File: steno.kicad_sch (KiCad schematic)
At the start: 16 parts, among them J1 USB_C_Receptacle_USB2.0_14P, U2 AP2127N-3.3, U3 W25Q16JVSS

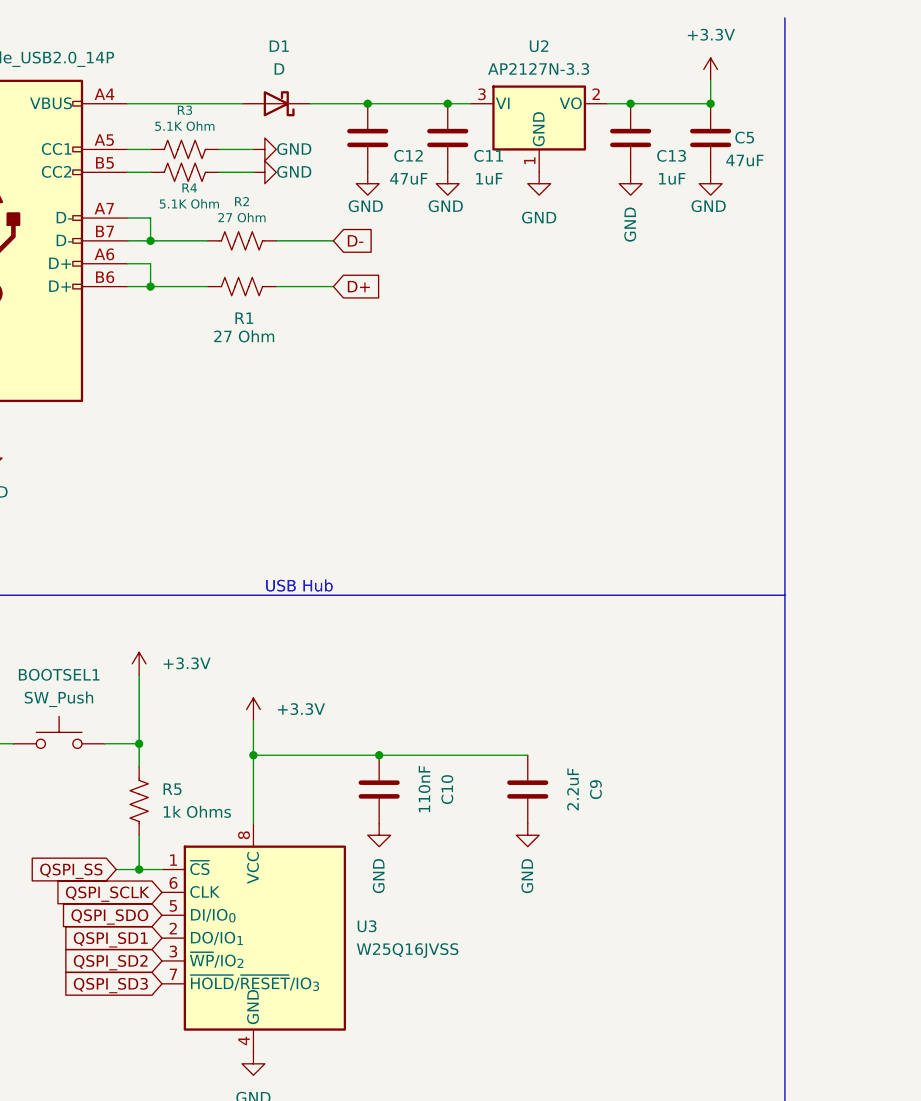
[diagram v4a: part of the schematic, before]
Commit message: Fixing buttons / Transitioning to new computer.
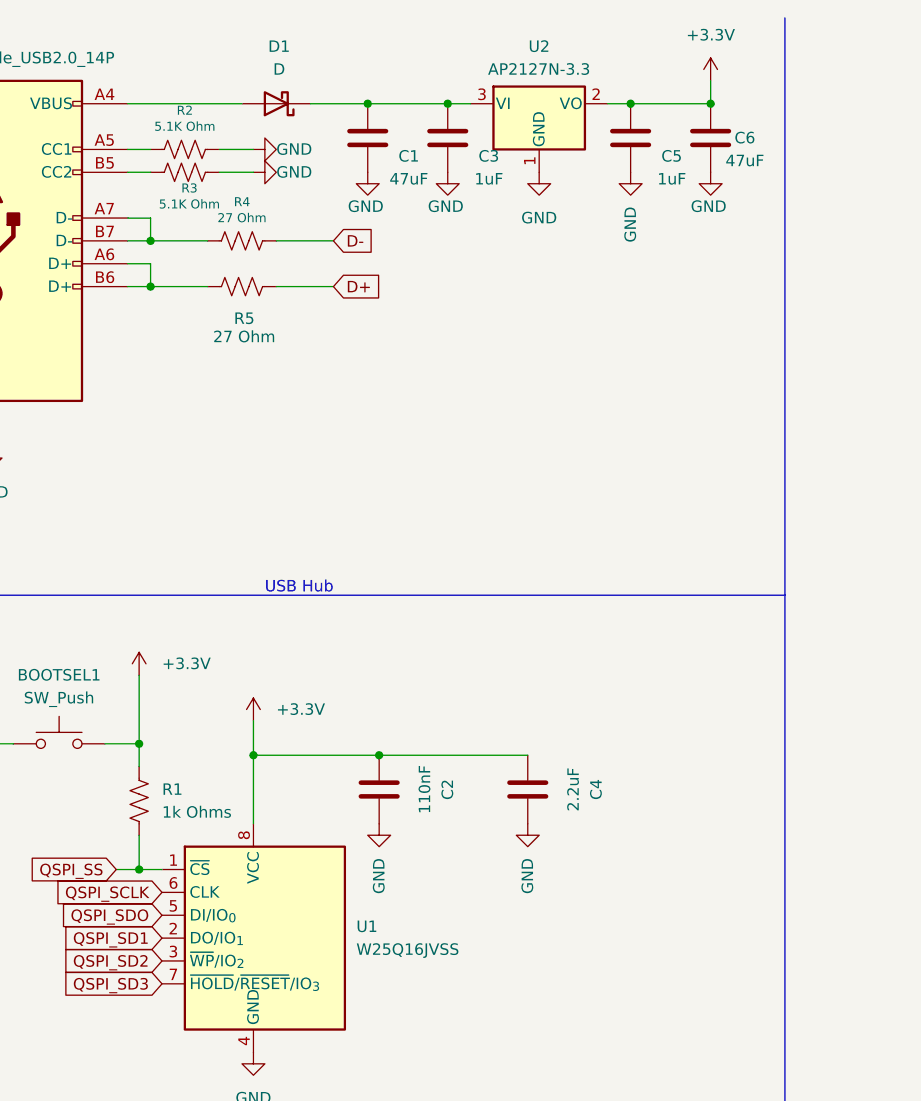
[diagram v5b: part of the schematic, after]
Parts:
- BOOTSEL1: footprint ScottoKeebs_Components:Button_MJTP1243 -> 3rd_party_footprints:SW4_PTS815 SJM 250 SMTR LFS_CNK
- renumbered C12 to C1, C10 to C2, C11 to C3, C9 to C4, C13 to C5, C5 to C6, R5 to R1, R3 to R2, R4 to R3, R2 to R4, R1 to R5, U3 to U1
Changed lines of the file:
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@@
 		(in_pos_files yes)
 		(dnp no)
-		(property "Reference" "C5"
+		(property "Reference" "C6"
 			(at 113.03 25.4 0)
 			(show_name no)
@@
 			(project "steno"
 				(path "/238e1d3b-9ec5-448b-85c7-386a29cd2631"
-					(reference "C5")
+					(reference "C6")
 					(unit 1)
 				)
@@
 		(in_pos_files yes)
 		(dnp no)
-		(property "Reference" "R3"
+		(property "Reference" "R2"
 			(at 50.8 22.352 90)
 			(show_name no)
@@
 			(project "steno"
 				(path "/238e1d3b-9ec5-448b-85c7-386a29cd2631"
-					(reference "R3")
+					(reference "R2")
 					(unit 1)
 				)
@@
 		(in_pos_files yes)
 		(dnp no)
-		(property "Reference" "C12"
+		(property "Reference" "C1"
 			(at 75.692 27.432 0)
 			(show_name no)
@@
 			(project "steno"
 				(path "/238e1d3b-9ec5-448b-85c7-386a29cd2631"
-					(reference "C12")
+					(reference "C1")
 					(unit 1)
 				)
@@
 		(in_pos_files yes)
 		(dnp no)
-		(property "Reference" "C13"
+		(property "Reference" "C5"
 			(at 104.902 27.432 0)
 			(show_name no)
@@
 			(project "steno"
 				(path "/238e1d3b-9ec5-448b-85c7-386a29cd2631"
-					(reference "C13")
+					(reference "C5")
 					(unit 1)
 				)
@@
 		(in_pos_files yes)
 		(dnp no)
-		(property "Reference" "C11"
+		(property "Reference" "C3"
 			(at 84.582 27.432 0)
 			(show_name no)
@@
 			(project "steno"
 				(path "/238e1d3b-9ec5-448b-85c7-386a29cd2631"
-					(reference "C11")
+					(reference "C3")
 					(unit 1)
 				)
@@
 		(in_pos_files yes)
 		(dnp no)
-		(property "Reference" "#PWR023"
+		(property "Reference" "#PWR02"
 			(at 26.67 102.87 0)
 			(hide yes)
@@
 			(project "steno"
 				(path "/238e1d3b-9ec5-448b-85c7-386a29cd2631"
-					(reference "#PWR023")
+					(reference "#PWR02")
 					(unit 1)
 				)
@@
 		(in_pos_files yes)
 		(dnp no)
-		(property "Reference" "R1"
+		(property "Reference" "R5"
 			(at 57.404 45.466 90)
 			(show_name no)
@@
 			(project "steno"
 				(path "/238e1d3b-9ec5-448b-85c7-386a29cd2631"
-					(reference "R1")
+					(reference "R5")
 					(unit 1)
 				)
@@
 		(in_pos_files yes)
 		(dnp no)
-		(property "Reference" "R4"
+		(property "Reference" "R3"
 			(at 51.308 30.988 90)
 			(show_name no)
@@
 			(project "steno"
 				(path "/238e1d3b-9ec5-448b-85c7-386a29cd2631"
-					(reference "R4")
+					(reference "R3")
 					(unit 1)
 				)
@@
 		(dnp no)
 		(fields_autoplaced yes)
-		(property "Reference" "#PWR027"
+		(property "Reference" "#PWR014"
 			(at 100.33 35.56 0)
 			(hide yes)
@@
 			(project "steno"
 				(path "/238e1d3b-9ec5-448b-85c7-386a29cd2631"
-					(reference "#PWR027")
+					(reference "#PWR014")
 					(unit 1)
 				)
@@
 		(in_pos_files yes)
 		(dnp no)
-		(property "Reference" "#PWR015"
+		(property "Reference" "#PWR06"
 			(at 64.77 29.21 0)
 			(hide yes)
@@
 			(project "steno"
 				(path "/238e1d3b-9ec5-448b-85c7-386a29cd2631"
-					(reference "#PWR015")
+					(reference "#PWR06")
 					(unit 1)
 				)
@@
 		(dnp no)
 		(fields_autoplaced yes)
-		(property "Reference" "#PWR024"
+		(property "Reference" "#PWR04"
 			(at 45.72 88.9 0)
 			(hide yes)
@@
 			(project "steno"
 				(path "/238e1d3b-9ec5-448b-85c7-386a29cd2631"
-					(reference "#PWR024")
+					(reference "#PWR04")
 					(unit 1)
 				)
@@
 		(dnp no)
 		(fields_autoplaced yes)
-		(property "Reference" "#PWR022"
+		(property "Reference" "#PWR010"
 			(at 72.39 107.95 0)
 			(hide yes)
@@
 			(project "steno"
 				(path "/238e1d3b-9ec5-448b-85c7-386a29cd2631"
-					(reference "#PWR022")
+					(reference "#PWR010")
 					(unit 1)
 				)
@@
 		(dnp no)
 		(fields_autoplaced yes)
-		(property "Reference" "#PWR011"
+		(property "Reference" "#PWR01"
 			(at 21.59 66.04 0)
 			(hide yes)
@@
 			(project "steno"
 				(path "/238e1d3b-9ec5-448b-85c7-386a29cd2631"
-					(reference "#PWR011")
+					(reference "#PWR01")
 					(unit 1)
 				)
@@
 		(dnp no)
 		(fields_autoplaced yes)
-		(property "Reference" "R5"
+		(property "Reference" "R1"
 			(at 48.26 97.7899 0)
 			(show_name no)
@@
 			(project "steno"
 				(path "/238e1d3b-9ec5-448b-85c7-386a29cd2631"
-					(reference "R5")
+					(reference "R1")
 					(unit 1)
 				)
@@
 		(in_pos_files yes)
 		(dnp no)
-		(property "Reference" "R2"
+		(property "Reference" "R4"
 			(at 57.15 32.512 90)
 			(show_name no)
@@
 			(project "steno"
 				(path "/238e1d3b-9ec5-448b-85c7-386a29cd2631"
-					(reference "R2")
+					(reference "R4")
 					(unit 1)
 				)
@@
 		(dnp no)
 		(fields_autoplaced yes)
-		(property "Reference" "#PWR010"
+		(property "Reference" "#PWR013"
 			(at 90.17 35.56 0)
 			(hide yes)
@@
 			(project "steno"
 				(path "/238e1d3b-9ec5-448b-85c7-386a29cd2631"
-					(reference "#PWR010")
+					(reference "#PWR013")
 					(unit 1)
 				)
@@
 		(dnp no)
 		(fields_autoplaced yes)
-		(property "Reference" "C10"
+		(property "Reference" "C2"
 			(at 80.01 97.79 90)
 			(show_name no)
@@
 			(project "steno"
 				(path "/238e1d3b-9ec5-448b-85c7-386a29cd2631"
-					(reference "C10")
+					(reference "C2")
 					(unit 1)
 				)
@@
 			)
 		)
-		(property "Footprint" "ScottoKeebs_Components:Button_MJTP1243"
+		(property "Footprint" "3rd_party_footprints:SW4_PTS815 SJM 250 SMTR LFS_CNK"
 			(at 36.83 87.63 0)
 			(hide yes)
@@
 		(dnp no)
 		(fields_autoplaced yes)
-		(property "Reference" "#PWR019"
+		(property "Reference" "#PWR07"
 			(at 58.42 93.98 0)
 			(hide yes)
@@
 			(project "steno"
 				(path "/238e1d3b-9ec5-448b-85c7-386a29cd2631"
-					(reference "#PWR019")
+					(reference "#PWR07")
 					(unit 1)
 				)
@@
 		(in_pos_files yes)
 		(dnp no)
-		(property "Reference" "#PWR014"
+		(property "Reference" "#PWR05"
 			(at 64.77 26.67 0)
 			(hide yes)
@@
 			(project "steno"
 				(path "/238e1d3b-9ec5-448b-85c7-386a29cd2631"
-					(reference "#PWR014")
+					(reference "#PWR05")
 					(unit 1)
 				)
@@
 		(in_pos_files yes)
 		(dnp no)
-		(property "Reference" "#PWR025"
+		(property "Reference" "#PWR011"
 			(at 80.01 35.56 0)
 			(hide yes)
@@
 			(project "steno"
 				(path "/238e1d3b-9ec5-448b-85c7-386a29cd2631"
-					(reference "#PWR025")
+					(reference "#PWR011")
 					(unit 1)
 				)
@@
 		(dnp no)
 		(fields_autoplaced yes)
-		(property "Reference" "C9"
+		(property "Reference" "C4"
 			(at 96.52 97.79 90)
 			(show_name no)
@@
 			(project "steno"
 				(path "/238e1d3b-9ec5-448b-85c7-386a29cd2631"
-					(reference "C9")
+					(reference "C4")
 					(unit 1)
 				)
@@
 		(dnp no)
 		(fields_autoplaced yes)
-		(property "Reference" "#PWR021"
+		(property "Reference" "#PWR012"
 			(at 88.9 107.95 0)
 			(hide yes)
@@
 			(project "steno"
 				(path "/238e1d3b-9ec5-448b-85c7-386a29cd2631"
-					(reference "#PWR021")
+					(reference "#PWR012")
 					(unit 1)
 				)
@@
 		(in_pos_files yes)
 		(dnp no)
-		(property "Reference" "#PWR026"
+		(property "Reference" "#PWR09"
 			(at 71.12 35.56 0)
 			(hide yes)
@@
 			(project "steno"
 				(path "/238e1d3b-9ec5-448b-85c7-386a29cd2631"
-					(reference "#PWR026")
+					(reference "#PWR09")
 					(unit 1)
 				)
@@
 		(in_pos_files yes)
 		(dnp no)
-		(property "Reference" "#PWR013"
+		(property "Reference" "#PWR016"
 			(at 109.22 35.56 0)
 			(hide yes)
@@
 			(project "steno"
 				(path "/238e1d3b-9ec5-448b-85c7-386a29cd2631"
-					(reference "#PWR013")
+					(reference "#PWR016")
 					(unit 1)
 				)
@@
 		(dnp no)
 		(fields_autoplaced yes)
-		(property "Reference" "U3"
+		(property "Reference" "U1"
 			(at 69.85 113.0299 0)
 			(show_name no)
@@
 			(project "steno"
 				(path "/238e1d3b-9ec5-448b-85c7-386a29cd2631"
-					(reference "U3")
+					(reference "U1")
 					(unit 1)
 				)
@@
 		(dnp no)
 		(fields_autoplaced yes)
-		(property "Reference" "#PWR020"
+		(property "Reference" "#PWR08"
 			(at 58.42 133.35 0)
 			(hide yes)
@@
 			(project "steno"
 				(path "/238e1d3b-9ec5-448b-85c7-386a29cd2631"
-					(reference "#PWR020")
+					(reference "#PWR08")
 					(unit 1)
 				)
@@
 		(dnp no)
 		(fields_autoplaced yes)
-		(property "Reference" "#PWR012"
+		(property "Reference" "#PWR015"
 			(at 109.22 22.86 0)
 			(hide yes)
@@
 			(project "steno"
 				(path "/238e1d3b-9ec5-448b-85c7-386a29cd2631"
-					(reference "#PWR012")
-					(unit 1)
-				)
+					(reference "#PWR015")
+					(unit 1)
+				)

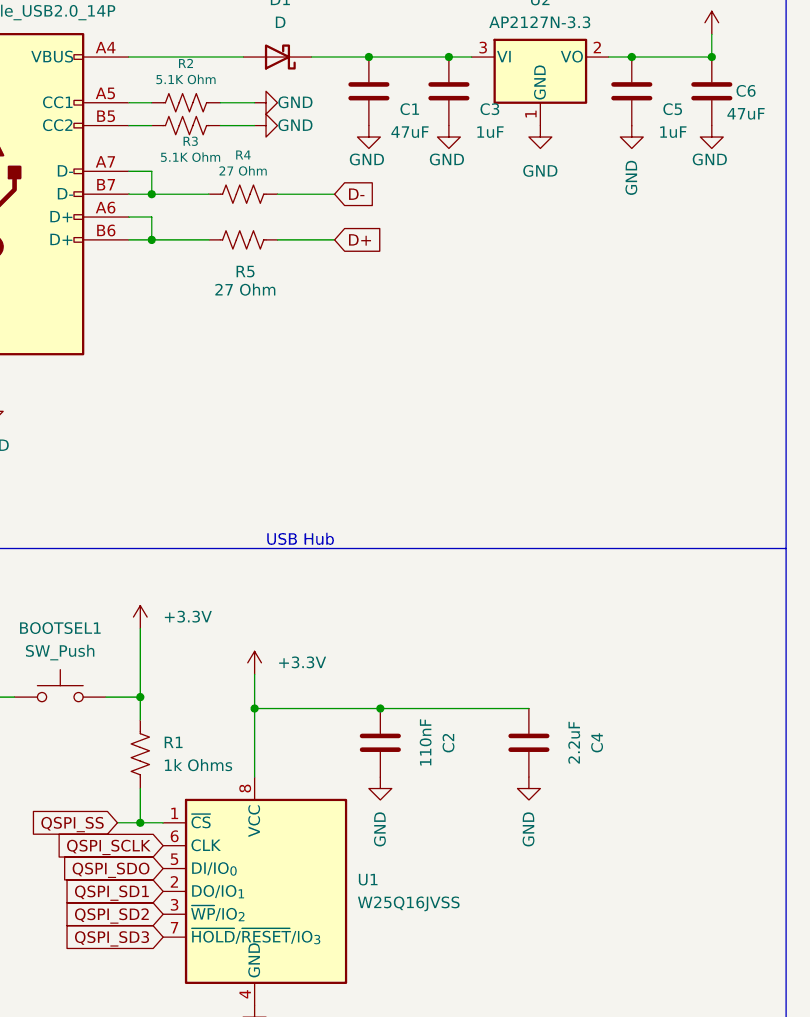
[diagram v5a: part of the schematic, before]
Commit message: added status LED / Potential final changes
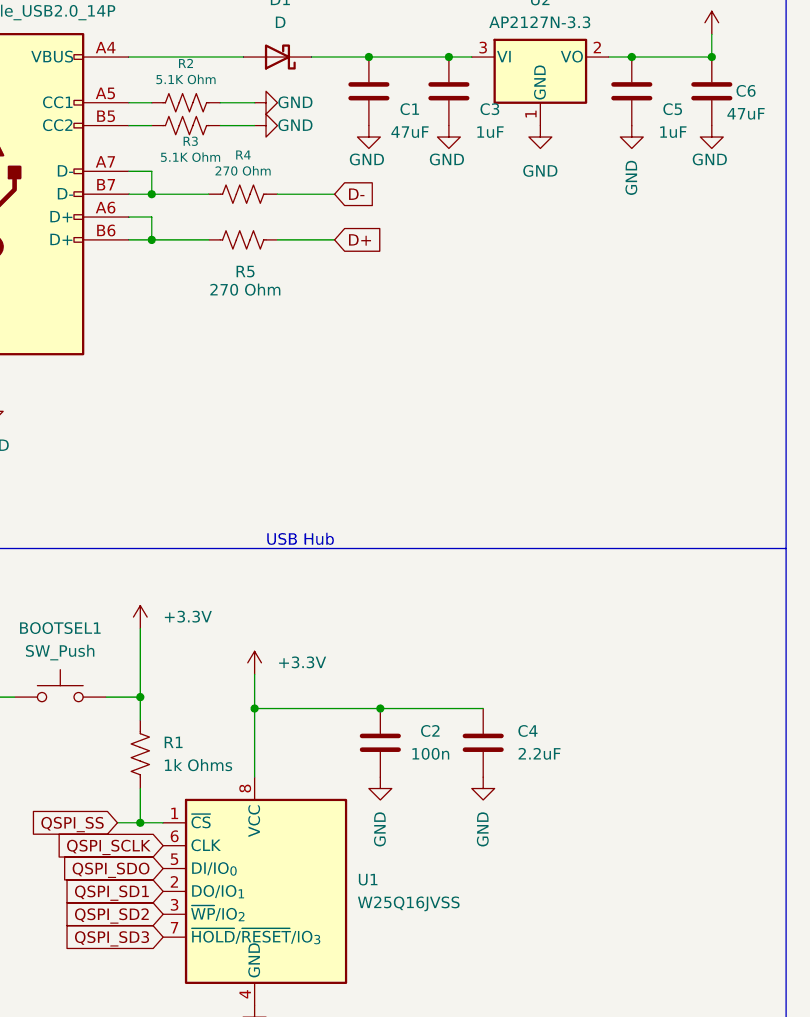
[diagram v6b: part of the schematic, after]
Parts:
- C2: value 110nF -> 100n
- R4, R5: value 27 Ohm -> 270 Ohm
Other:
- moved on the sheet: C4
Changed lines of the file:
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@@
+	)
+	(junction
+		(at 80.01 21.59)
+		(diameter 0)
+		(color 0 0 0 0)
+	)
+	(junction
+		(at 71.12 21.59)
+		(diameter 0)
+		(color 0 0 0 0)
+	)
+	(junction
+		(at 58.42 93.98)
+		(diameter 0)
+		(color 0 0 0 0)
+	)
+	(junction
+		(at 46.99 36.83)
+		(diameter 0)
+		(color 0 0 0 0)
+	)
+	(junction
+		(at 45.72 106.68)
+		(diameter 0)
+		(color 0 0 0 0)
 	)
 	(junction
@@
 	)
 	(junction
-		(at 80.01 21.59)
-		(diameter 0)
-		(color 0 0 0 0)
-	)
-	(junction
-		(at 71.12 21.59)
-		(diameter 0)
-		(color 0 0 0 0)
-	)
-	(junction
-		(at 58.42 93.98)
-		(diameter 0)
-		(color 0 0 0 0)
-	)
-	(junction
-		(at 46.99 36.83)
-		(diameter 0)
-		(color 0 0 0 0)
-	)
-	(junction
-		(at 45.72 106.68)
-		(diameter 0)
-		(color 0 0 0 0)
-	)
-	(junction
 		(at 45.72 92.71)
 		(diameter 0)
@@
 	(wire
 		(pts
-			(xy 72.39 93.98) (xy 88.9 93.98)
+			(xy 72.39 93.98) (xy 83.82 93.98)
 		)
 		(stroke
@@
 			)
 		)
-		(property "Value" "27 Ohm"
+		(property "Value" "270 Ohm"
 			(at 57.404 47.498 90)
 			(show_name no)
@@
 			)
 		)
-		(property "Value" "27 Ohm"
+		(property "Value" "270 Ohm"
 			(at 57.15 34.29 90)
 			(show_name no)
@@
 		(in_pos_files yes)
 		(dnp no)
-		(fields_autoplaced yes)
 		(property "Reference" "C2"
-			(at 80.01 97.79 90)
-			(show_name no)
-			(do_not_autoplace no)
-			(effects
-				(font
-					(size 1.27 1.27)
-				)
-			)
-		)
-		(property "Value" "110nF"
-			(at 77.47 97.79 90)
+			(at 77.978 96.52 0)
+			(show_name no)
+			(do_not_autoplace no)
+			(effects
+				(font
+					(size 1.27 1.27)
+				)
+			)
+		)
+		(property "Value" "100n"
+			(at 77.978 99.06 0)
 			(show_name no)
 			(do_not_autoplace no)
@@
 	(symbol
 		(lib_id "Device:C")
-		(at 88.9 97.79 0)
+		(at 83.82 97.79 0)
 		(unit 1)
 		(body_style 1)
@@
 		(fields_autoplaced yes)
 		(property "Reference" "C4"
-			(at 96.52 97.79 90)
-			(show_name no)
-			(do_not_autoplace no)
-			(effects
-				(font
-					(size 1.27 1.27)
-				)
+			(at 87.63 96.5199 0)
+			(show_name no)
+			(do_not_autoplace no)
+			(effects
+				(font
+					(size 1.27 1.27)
+				)
+				(justify left)
 			)
 		)
 		(property "Value" "2.2uF"
-			(at 93.98 97.79 90)
-			(show_name no)
-			(do_not_autoplace no)
-			(effects
-				(font
-					(size 1.27 1.27)
-				)
+			(at 87.63 99.0599 0)
+			(show_name no)
+			(do_not_autoplace no)
+			(effects
+				(font
+					(size 1.27 1.27)
+				)
+				(justify left)
 			)
 		)
 		(property "Footprint" "Capacitor_SMD:C_0402_1005Metric_Pad0.74x0.62mm_HandSolder"
-			(at 89.8652 101.6 0)
+			(at 84.7852 101.6 0)
 			(hide yes)
 			(show_name no)
@@
 		)
 		(property "Datasheet" ""
-			(at 88.9 97.79 0)
+			(at 83.82 97.79 0)
 			(hide yes)
 			(show_name no)
@@
 		)
 		(property "Description" "Unpolarized capacitor"
-			(at 88.9 97.79 0)
+			(at 83.82 97.79 0)
 			(hide yes)
 			(show_name no)
@@
 	(symbol
 		(lib_id "power:GND")
-		(at 88.9 101.6 0)
+		(at 83.82 101.6 0)
 		(unit 1)
 		(body_style 1)
@@
 		(fields_autoplaced yes)
 		(property "Reference" "#PWR012"
-			(at 88.9 107.95 0)
+			(at 83.82 107.95 0)
 			(hide yes)
 			(show_name no)
@@
 		)
 		(property "Value" "GND"
-			(at 88.9001 105.41 90)
+			(at 83.8201 105.41 90)
 			(show_name no)
 			(do_not_autoplace no)
@@
 		)
 		(property "Footprint" ""
-			(at 88.9 101.6 0)
+			(at 83.82 101.6 0)
 			(hide yes)
 			(show_name no)
@@
 		)
 		(property "Datasheet" ""
-			(at 88.9 101.6 0)
+			(at 83.82 101.6 0)
 			(hide yes)
 			(show_name no)
@@
 		)
 		(property "Description" "Power symbol creates a global label with name \"GND\" , ground"
-			(at 88.9 101.6 0)
-			(hide yes)
-			(show_name no)
+			(at 83.82 101.6 0)
+			(hide yes)
+			(show_name no)
